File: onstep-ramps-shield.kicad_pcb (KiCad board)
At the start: 2 copper layers, 116.8 x 67.3 mm, 32 parts

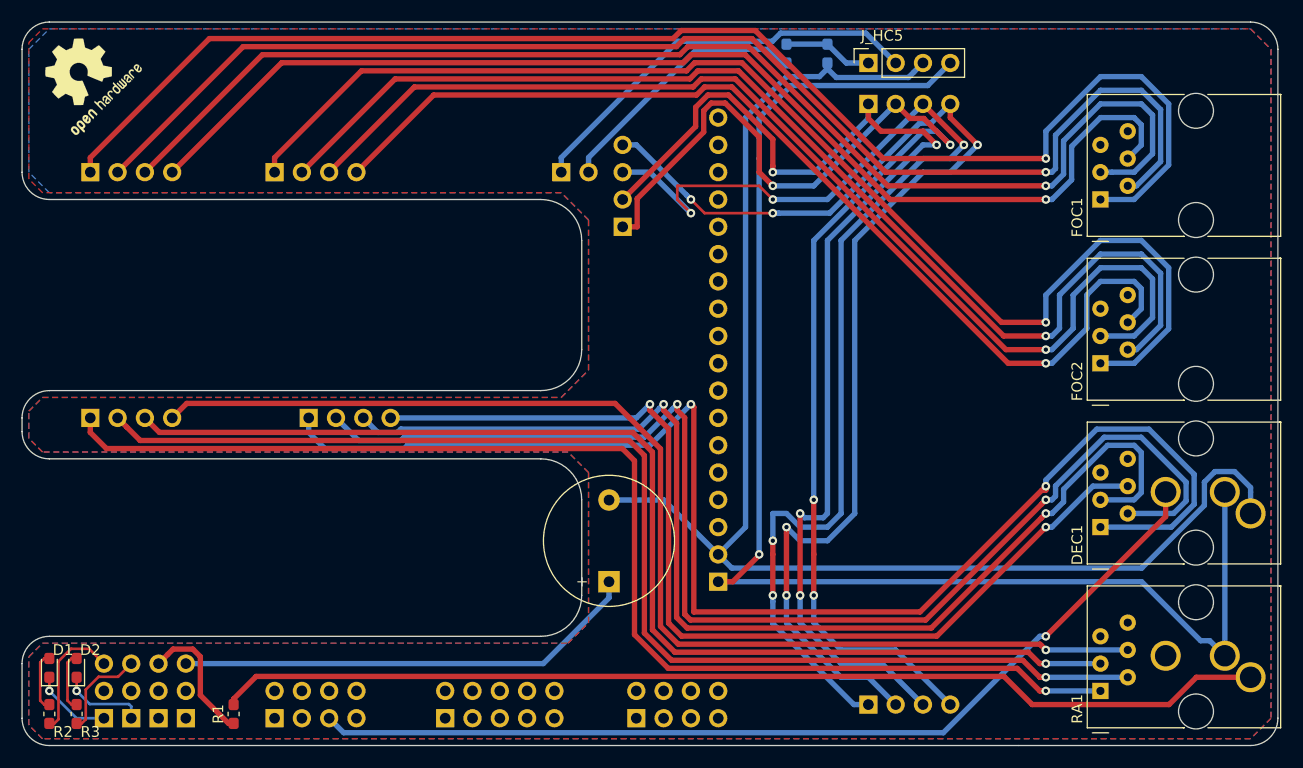
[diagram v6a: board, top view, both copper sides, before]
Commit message: Add silkscreen version info
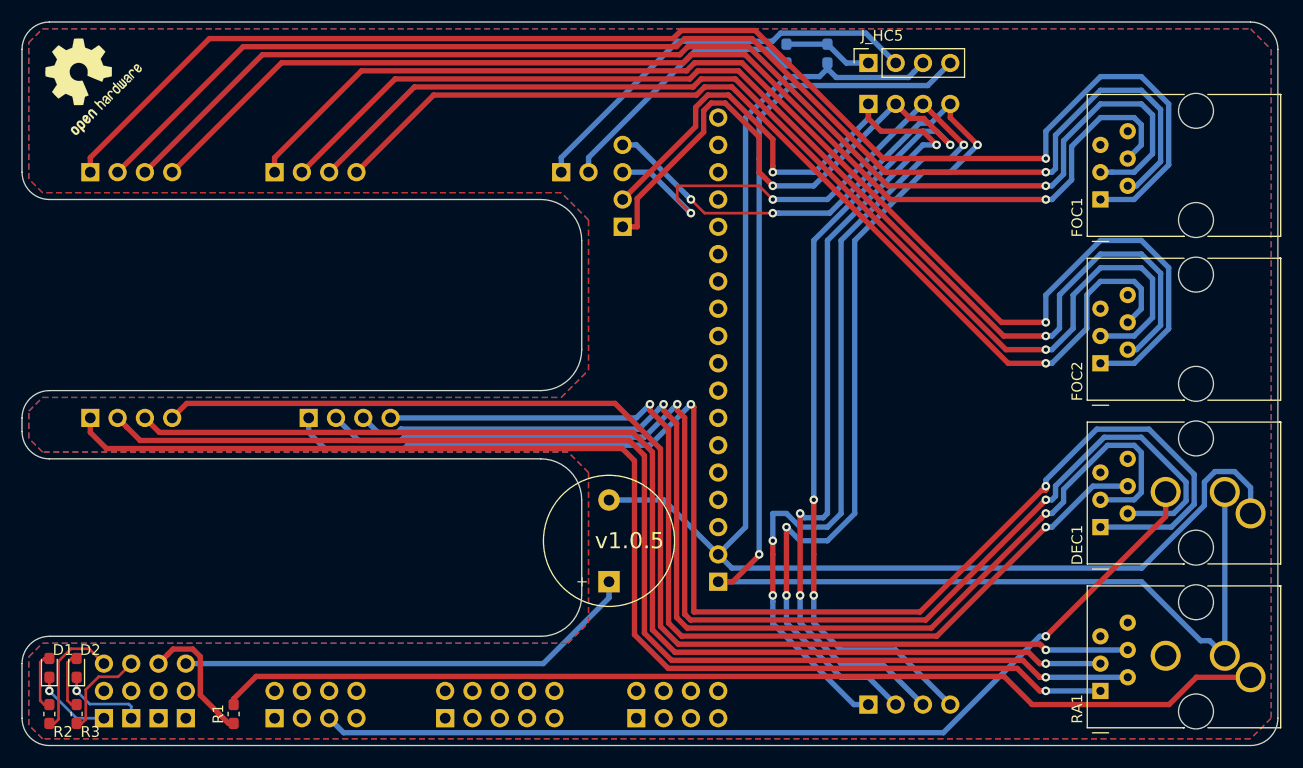
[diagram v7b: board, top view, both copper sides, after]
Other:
- board text added: "https://github.com/philipgatzka/onstep-ramps-shield"
- board text added: "v1.0.5"
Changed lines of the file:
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@@
   (general
     (thickness 1.6002)
-    (drawings 29)
+    (drawings 31)
     (tracks 482)
     (zones 0)
@@
       (rotate (xyz 0 0 0))
     )
+  )
+  (gr_text v1.0.5 (at 142.875 99.06) (layer F.SilkS)
+    (effects (font (size 1.5 1.5) (thickness 0.2)))
+  )
+  (gr_text https://github.com/philipgatzka/onstep-ramps-shield (at 120.65 54.61 180) (layer B.SilkS)
+    (effects (font (size 1.5 1.5) (thickness 0.2)) (justify mirror))
   )
   (gr_arc (start 134.62 104.14) (end 134.62 107.95) (angle -90) (layer Edge.Cuts) (width 0.1))
@@
         (xy 86.995 109.855) (xy 88.265 108.585) (xy 137.16 108.585) (xy 139.065 106.68) (xy 139.065 92.71)
         (xy 137.16 90.805) (xy 88.265 90.805) (xy 86.995 89.535) (xy 86.995 86.995) (xy 88.265 85.725)
-        (xy 136.525 85.725) (xy 139.065 83.185) (xy 139.065 69.215) (xy 136.525 66.675) (xy 88.9 66.675)
-        (xy 86.995 64.77) (xy 86.995 53.34) (xy 88.9 51.435) (xy 200.66 51.435)
+        (xy 136.525 85.725) (xy 139.065 83.185) (xy 139.065 69.215) (xy 136.525 66.675) (xy 88.265 66.675)
+        (xy 86.995 65.405) (xy 86.995 52.705) (xy 88.265 51.435) (xy 200.66 51.435)
       )
     )

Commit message: Update distances
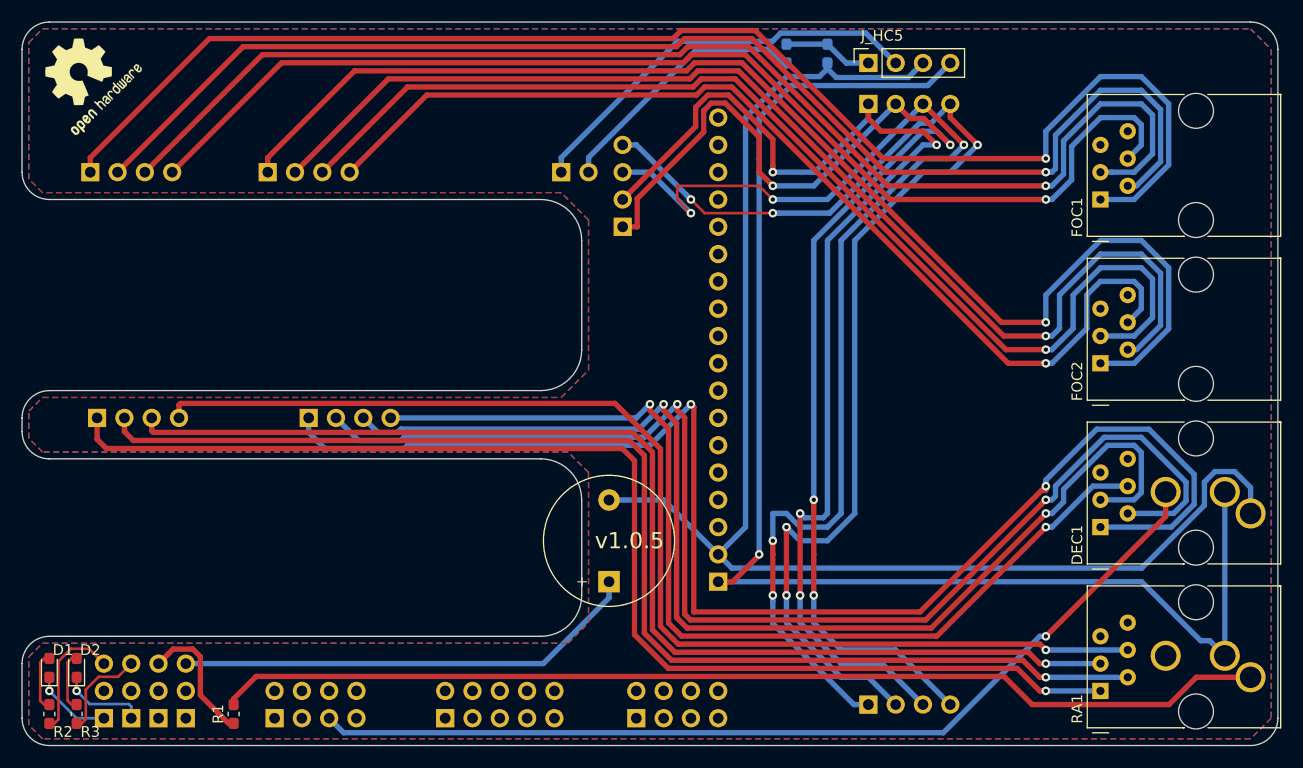
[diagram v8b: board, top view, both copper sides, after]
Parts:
- moved J_FOC2 0.64 mm to (109.2, 64.8)
- moved J_RA1 0.64 mm to (93.3, 87.6)
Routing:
- net E1_2B: track 117.2 -> 117.9 mm
- net E1_2A: track 108.6 -> 109.2 mm
- net E1_1B: track 95.9 -> 96.5 mm
- net E1_1A: track 105.2 -> 105.8 mm
